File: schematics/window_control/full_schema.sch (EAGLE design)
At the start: 73 parts, among them J1 MTR-SERVO-FS5103B, J10 USBASP_PIN, J2 J2, J3 J2, J4 J2, J5 J2, J6 J2, J7 J2, J8 J2, J9 J2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

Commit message: Added button borders and nominals
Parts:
- removed SB4: SB-NO, my_devices:SB-NO
- SB1: value SB-NC -> KLS7-DS-01-B-00
- SB2, SB3: value SB-NO -> FSMRA6JH
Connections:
- removed net GPIO_TS_WINDOW_AUTO: SB4.P$1, U1.IO12
- net GND: no longer SB4.P$2
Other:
- moved on the sheet: J2, J3, J4, J5
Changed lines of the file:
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@@
 <part name="C9" library="my_devices" deviceset="C-1" device="" value="0.1 uF"/>
 <part name="J10" library="my_devices" deviceset="USBASP_PIN" device=""/>
-<part name="SB1" library="my_devices" deviceset="SB-NC" device=""/>
-<part name="SB2" library="my_devices" deviceset="SB-NO" device=""/>
-<part name="SB3" library="my_devices" deviceset="SB-NO" device=""/>
-<part name="SB4" library="my_devices" deviceset="SB-NO" device=""/>
+<part name="SB1" library="my_devices" deviceset="SB-NC" device="" value="KLS7-DS-01-B-00"/>
+<part name="SB2" library="my_devices" deviceset="SB-NO" device="" value="FSMRA6JH"/>
+<part name="SB3" library="my_devices" deviceset="SB-NO" device="" value="FSMRA6JH"/>
 <part name="GND9" library="supply1" library_urn="urn:adsk.eagle:library:371" deviceset="GND" device=""/>
 </parts>
@@
 <attribute name="VALUE" x="-222.25" y="44.45" size="1.778" layer="94"/>
 </instance>
-<instance part="J2" gate="G$1" x="73.66" y="142.24" smashed="yes" rot="R180" grouprefs="INDOOR_TO_OUTDOOR_CABEL">
-<attribute name="NAME" x="76.2" y="140.335" size="1.778" layer="94" rot="R180"/>
-<attribute name="VALUE" x="76.2" y="149.86" size="1.778" layer="94" rot="R180"/>
-</instance>
-<instance part="J4" gate="G$1" x="78.74" y="144.78" smashed="yes" grouprefs="INDOOR_TO_OUTDOOR_CABEL">
-<attribute name="NAME" x="76.2" y="146.685" size="1.778" layer="94"/>
-<attribute name="VALUE" x="76.2" y="137.16" size="1.778" layer="94"/>
+<instance part="J2" gate="G$1" x="81.28" y="142.24" smashed="yes" rot="R180" grouprefs="INDOOR_TO_OUTDOOR_CABEL">
+<attribute name="NAME" x="83.82" y="140.335" size="1.778" layer="94" rot="R180"/>
+<attribute name="VALUE" x="83.82" y="149.86" size="1.778" layer="94" rot="R180"/>
+</instance>
+<instance part="J4" gate="G$1" x="86.36" y="144.78" smashed="yes" grouprefs="INDOOR_TO_OUTDOOR_CABEL">
+<attribute name="NAME" x="83.82" y="146.685" size="1.778" layer="94"/>
+<attribute name="VALUE" x="83.82" y="137.16" size="1.778" layer="94"/>
 </instance>
 <instance part="J6" gate="G$1" x="129.54" y="142.24" smashed="yes" rot="R180" grouprefs="INDOOR_TO_OUTDOOR_CABEL">
@@
 <attribute name="VALUE" x="134.62" y="137.16" size="1.778" layer="94"/>
 </instance>
-<instance part="GND5" gate="1" x="60.96" y="139.7" smashed="yes" grouprefs="INDOOR_TO_OUTDOOR_CABEL">
-<attribute name="VALUE" x="58.42" y="137.16" size="1.778" layer="96"/>
+<instance part="GND5" gate="1" x="71.12" y="139.7" smashed="yes" grouprefs="INDOOR_TO_OUTDOOR_CABEL">
+<attribute name="VALUE" x="68.58" y="137.16" size="1.778" layer="96"/>
 </instance>
 <instance part="C6" gate="G$1" x="162.56" y="142.24" smashed="yes" rot="R270" grouprefs="INDOOR_TO_OUTDOOR_CABEL">
@@
 <attribute name="VALUE" x="132.08" y="121.92" size="1.778" layer="94" rot="R180"/>
 </instance>
-<instance part="J5" gate="G$1" x="78.74" y="116.84" smashed="yes" grouprefs="INDOOR_TO_OUTDOOR_CABEL">
-<attribute name="NAME" x="76.2" y="118.745" size="1.778" layer="94"/>
-<attribute name="VALUE" x="76.2" y="109.22" size="1.778" layer="94"/>
-</instance>
-<instance part="J3" gate="G$1" x="73.66" y="114.3" smashed="yes" rot="R180" grouprefs="INDOOR_TO_OUTDOOR_CABEL">
-<attribute name="NAME" x="76.2" y="112.395" size="1.778" layer="94" rot="R180"/>
-<attribute name="VALUE" x="76.2" y="121.92" size="1.778" layer="94" rot="R180"/>
-</instance>
-<instance part="GND6" gate="1" x="60.96" y="111.76" smashed="yes" grouprefs="INDOOR_TO_OUTDOOR_CABEL">
-<attribute name="VALUE" x="58.42" y="109.22" size="1.778" layer="96"/>
+<instance part="J5" gate="G$1" x="86.36" y="116.84" smashed="yes" grouprefs="INDOOR_TO_OUTDOOR_CABEL">
+<attribute name="NAME" x="83.82" y="118.745" size="1.778" layer="94"/>
+<attribute name="VALUE" x="83.82" y="109.22" size="1.778" layer="94"/>
+</instance>
+<instance part="J3" gate="G$1" x="81.28" y="114.3" smashed="yes" rot="R180" grouprefs="INDOOR_TO_OUTDOOR_CABEL">
+<attribute name="NAME" x="83.82" y="112.395" size="1.778" layer="94" rot="R180"/>
+<attribute name="VALUE" x="83.82" y="121.92" size="1.778" layer="94" rot="R180"/>
+</instance>
+<instance part="GND6" gate="1" x="71.12" y="111.76" smashed="yes" grouprefs="INDOOR_TO_OUTDOOR_CABEL">
+<attribute name="VALUE" x="68.58" y="109.22" size="1.778" layer="96"/>
 </instance>
 <instance part="R6" gate="G$1" x="-172.72" y="109.22" smashed="yes" rot="R90" grouprefs="ESP">
@@
 <attribute name="NAME" x="-30.48" y="-17.78" size="1.778" layer="94"/>
 <attribute name="VALUE" x="-30.48" y="-20.32" size="1.778" layer="94"/>
-</instance>
-<instance part="SB4" gate="G$1" x="-25.4" y="-35.56" smashed="yes" grouprefs="OPEN-CLOSE">
-<attribute name="NAME" x="-30.48" y="-38.1" size="1.778" layer="94"/>
-<attribute name="VALUE" x="-30.48" y="-40.64" size="1.778" layer="94"/>
 </instance>
 <instance part="GND9" gate="1" x="-7.62" y="-17.78" smashed="yes" grouprefs="OPEN-CLOSE">
@@
 <pinref part="GND5" gate="1" pin="GND"/>
 <pinref part="J2" gate="G$1" pin="PIN_1"/>
-<wire x1="60.96" y1="142.24" x2="66.04" y2="142.24" width="0.1524" layer="91" grouprefs="INDOOR_TO_OUTDOOR_CABEL"/>
+<wire x1="73.66" y1="142.24" x2="71.12" y2="142.24" width="0.1524" layer="91"/>
 </segment>
 <segment>
 <pinref part="GND6" gate="1" pin="GND"/>
 <pinref part="J3" gate="G$1" pin="PIN_1"/>
-<wire x1="60.96" y1="114.3" x2="66.04" y2="114.3" width="0.1524" layer="91" grouprefs="INDOOR_TO_OUTDOOR_CABEL"/>
+<wire x1="71.12" y1="114.3" x2="73.66" y2="114.3" width="0.1524" layer="91" grouprefs="INDOOR_TO_OUTDOOR_CABEL"/>
 </segment>
 <segment>
@@
 </segment>
 <segment>
-<pinref part="SB4" gate="G$1" pin="P$2"/>
 <pinref part="SB3" gate="G$1" pin="P$2"/>
-<wire x1="-15.24" y1="-35.56" x2="-15.24" y2="-15.24" width="0.1524" layer="91" grouprefs="OPEN-CLOSE"/>
 <pinref part="SB2" gate="G$1" pin="P$2"/>
 <wire x1="-15.24" y1="5.08" x2="-15.24" y2="-15.24" width="0.1524" layer="91" grouprefs="OPEN-CLOSE"/>
@@
 </segment>
 </net>
-<net name="GPIO_TS_WINDOW_AUTO" class="0">
-<segment>
-<wire x1="-35.56" y1="-35.56" x2="-71.12" y2="-35.56" width="0.1524" layer="91" grouprefs="OPEN-CLOSE"/>
-<label x="-71.12" y="-35.56" size="1.778" layer="95" grouprefs="OPEN-CLOSE"/>
-<pinref part="SB4" gate="G$1" pin="P$1"/>
-</segment>
-<segment>
-<pinref part="U1" gate="G$1" pin="IO12"/>
-<wire x1="-236.22" y1="119.38" x2="-261.62" y2="119.38" width="0.1524" layer="91" grouprefs="ESP"/>
-<label x="-274.32" y="119.38" size="1.778" layer="95" grouprefs="ESP"/>
-</segment>
-</net>
 <net name="N$9" class="0">
 <segment>
 <pinref part="J4" gate="G$1" pin="PIN_1"/>
 <pinref part="J6" gate="G$1" pin="PIN_2"/>
-<wire x1="86.36" y1="144.78" x2="121.92" y2="144.78" width="0.1524" layer="91" grouprefs="INDOOR_TO_OUTDOOR_CABEL"/>
+<wire x1="93.98" y1="144.78" x2="121.92" y2="144.78" width="0.1524" layer="91" grouprefs="INDOOR_TO_OUTDOOR_CABEL"/>
 </segment>
 </net>
@@
 <pinref part="J4" gate="G$1" pin="PIN_2"/>
 <pinref part="J6" gate="G$1" pin="PIN_1"/>
-<wire x1="86.36" y1="142.24" x2="121.92" y2="142.24" width="0.1524" layer="91" grouprefs="INDOOR_TO_OUTDOOR_CABEL"/>
+<wire x1="93.98" y1="142.24" x2="121.92" y2="142.24" width="0.1524" layer="91" grouprefs="INDOOR_TO_OUTDOOR_CABEL"/>
 </segment>
 </net>
@@
 <pinref part="J5" gate="G$1" pin="PIN_1"/>
 <pinref part="J7" gate="G$1" pin="PIN_2"/>
-<wire x1="86.36" y1="116.84" x2="121.92" y2="116.84" width="0.1524" layer="91" grouprefs="INDOOR_TO_OUTDOOR_CABEL"/>
+<wire x1="93.98" y1="116.84" x2="121.92" y2="116.84" width="0.1524" layer="91" grouprefs="INDOOR_TO_OUTDOOR_CABEL"/>
 </segment>
 </net>
@@
 <pinref part="J5" gate="G$1" pin="PIN_2"/>
 <pinref part="J7" gate="G$1" pin="PIN_1"/>
-<wire x1="86.36" y1="114.3" x2="121.92" y2="114.3" width="0.1524" layer="91" grouprefs="INDOOR_TO_OUTDOOR_CABEL"/>
+<wire x1="93.98" y1="114.3" x2="121.92" y2="114.3" width="0.1524" layer="91" grouprefs="INDOOR_TO_OUTDOOR_CABEL"/>
 </segment>
 </net>
@@
 <segment>
 <pinref part="J3" gate="G$1" pin="PIN_2"/>
-<wire x1="66.04" y1="116.84" x2="45.72" y2="116.84" width="0.1524" layer="91" grouprefs="INDOOR_TO_OUTDOOR_CABEL"/>
+<wire x1="73.66" y1="116.84" x2="45.72" y2="116.84" width="0.1524" layer="91" grouprefs="INDOOR_TO_OUTDOOR_CABEL"/>
 <label x="43.18" y="116.84" size="1.778" layer="95" grouprefs="INDOOR_TO_OUTDOOR_CABEL"/>
 </segment>
@@
 <pinref part="SB1" gate="G$1" pin="P$2"/>
 <pinref part="J2" gate="G$1" pin="PIN_2"/>
-<wire x1="63.5" y1="144.78" x2="66.04" y2="144.78" width="0.1524" layer="91" grouprefs="INDOOR_TO_OUTDOOR_CABEL"/>
-</segment>
-</net>
+<wire x1="63.5" y1="144.78" x2="73.66" y2="144.78" width="0.1524" layer="91" grouprefs="INDOOR_TO_OUTDOOR_CABEL"/>
+</segment>
+</net>

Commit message: Start working under first border
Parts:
- SB1: value KLS7-DS-01-B-00 -> FSMRA6JH; device my_devices:SB-NC -> my_devices:SB-NO
- SB3: value FSMRA6JH -> KLS7-DS-01-B-00; device my_devices:SB-NO -> my_devices:SB-NC
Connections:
- net +5V: now also SB3.P$1; no longer SB1.P$1
- net GND: now also SB1.P$2; no longer SB3.P$2
- net GPIO_TS_WINDOW_CLOSE: now also SB2.P$1, U1.IO15; no longer SB3.P$1, U1.IO27
- net GPIO_TS_WINDOW_OPEN: now also SB1.P$1, U1.IO4; no longer SB2.P$1, U1.IO14
- net N$16: now also SB3.P$2; no longer SB1.P$2
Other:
- moved on the sheet: D1, Q1, R1, R2, R6, SB1, SB2, SB3

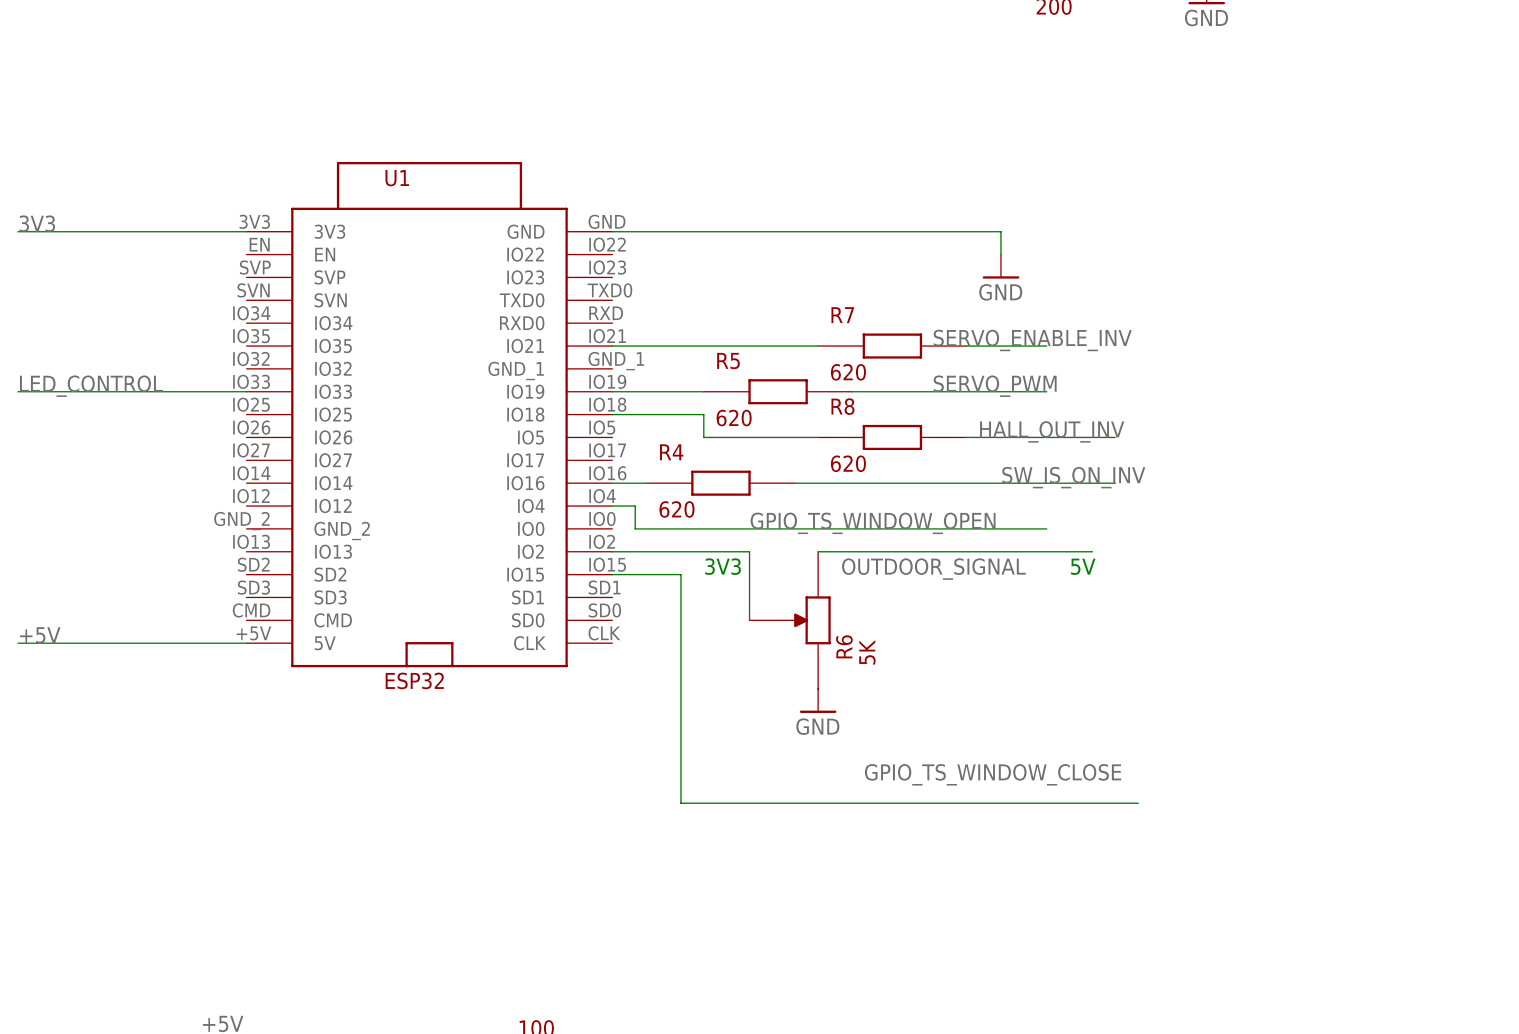
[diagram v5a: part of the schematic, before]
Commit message: hear handle module & indoor servo module assembled and checked
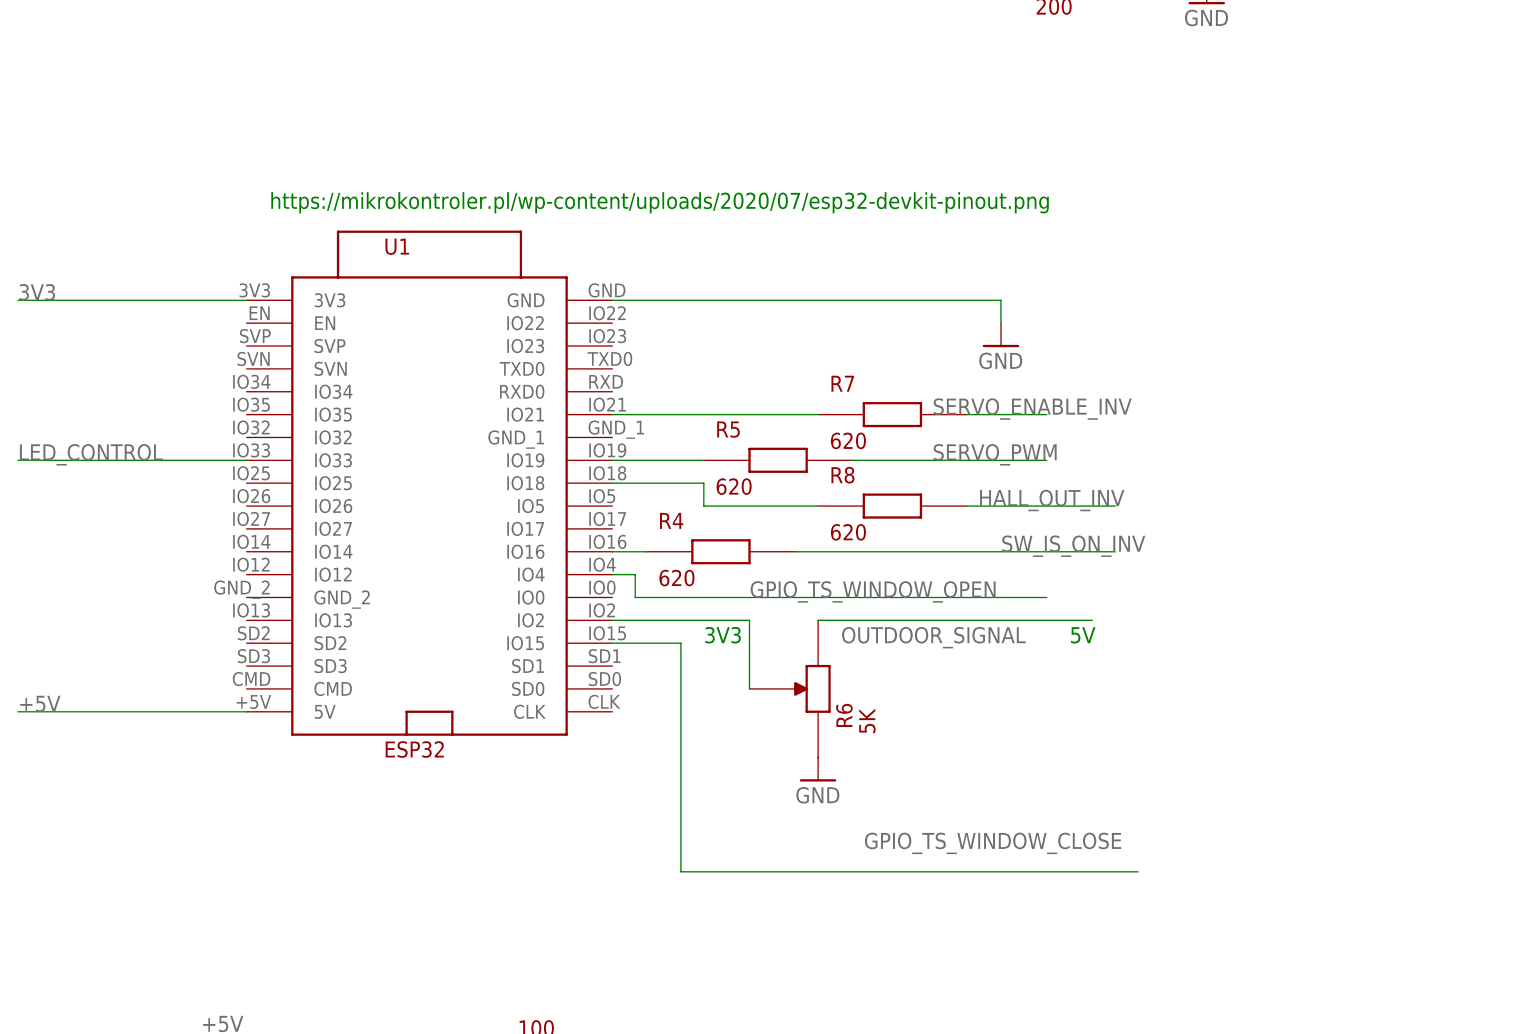
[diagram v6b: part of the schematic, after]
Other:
- note added: "https://mikrokontroler.pl/wp-content/uploads/2020/07/esp32-devkit-pinout.png"
- moved on the sheet: R4, R5, R6, R7, R8, U1
